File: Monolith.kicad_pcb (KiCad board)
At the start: 2 copper layers, 89.9 x 42.7 mm, 80 parts, among them IC1 HT7550-1, J1 USB_B_Micro, J2 Conn_01x11, J3 Conn_01x11, J4 Conn_01x02, J5 Conn_01x02, J6 Conn_01x07, Q1 BC818, Q2 BC818, U1 ADS1299IPAGR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

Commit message: fix pick and place stuff
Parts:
- C19, C22: footprint Capacitor_SMD:C_0603_1608Metric -> Capacitor_SMD:C_0805_2012Metric
- moved C19 1.73 mm to (232.9, 129.0)
- moved C22 1.14 mm to (202.8, 135.1)
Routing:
- net /AVSS: track 109.7 -> 98.5 mm
- net GND: track 268.6 -> 262.0 mm
- net Net-(U1-VREFN): track 9.04 -> 12.0 mm, vias 0 -> 2
- net +3V3: track 206.8 -> 208.1 mm
- net Net-(U1-VREFP): track 9.23 -> 9.80 mm
- net Net-(U1-VCAP4): track 7.40 -> 7.92 mm, vias 0 -> 2

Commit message: fix capacitor array footprint
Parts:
- C22: footprint Capacitor_SMD:C_0805_2012Metric -> Capacitor_SMD:C_0603_1608Metric
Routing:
- net /AVSS: track 98.5 -> 108.6 mm
- net /IN8P: track 19.5 -> 21.3 mm
- net GND: track 262.0 -> 263.6 mm
- net /INSRB2: track 21.9 -> 20.8 mm
- net /IN8N: track 16.9 -> 17.5 mm
- net /IN5N: track 14.6 -> 15.1 mm

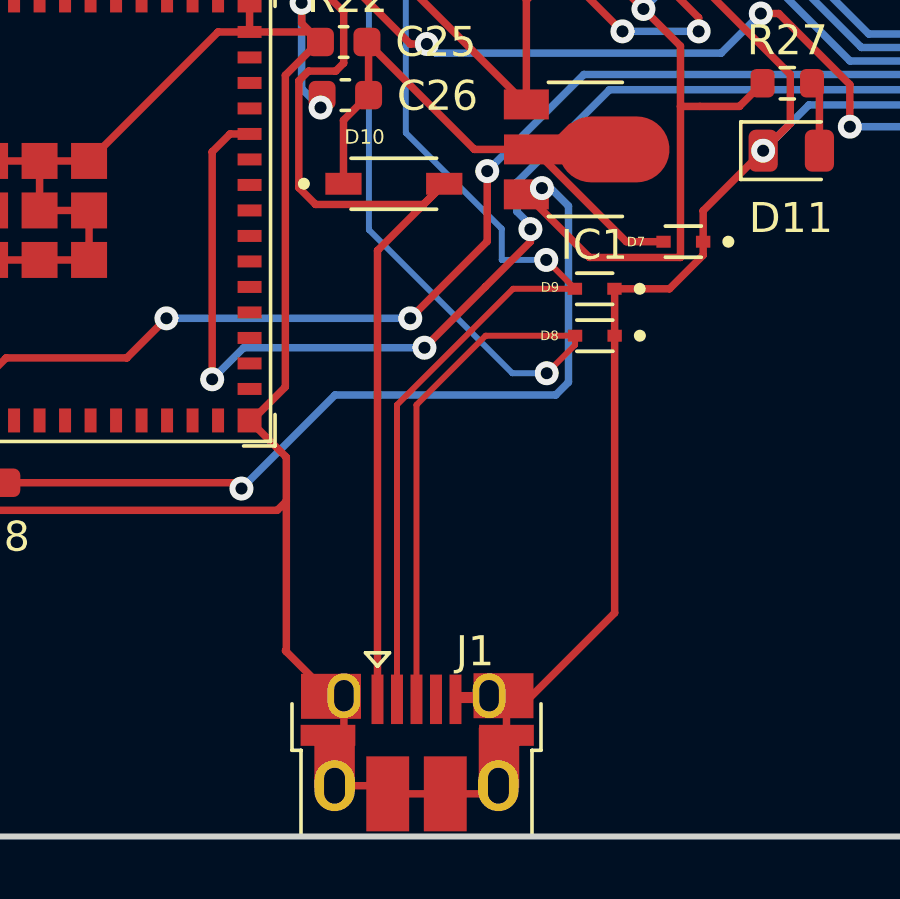
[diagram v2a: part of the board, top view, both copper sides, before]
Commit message: fix usb
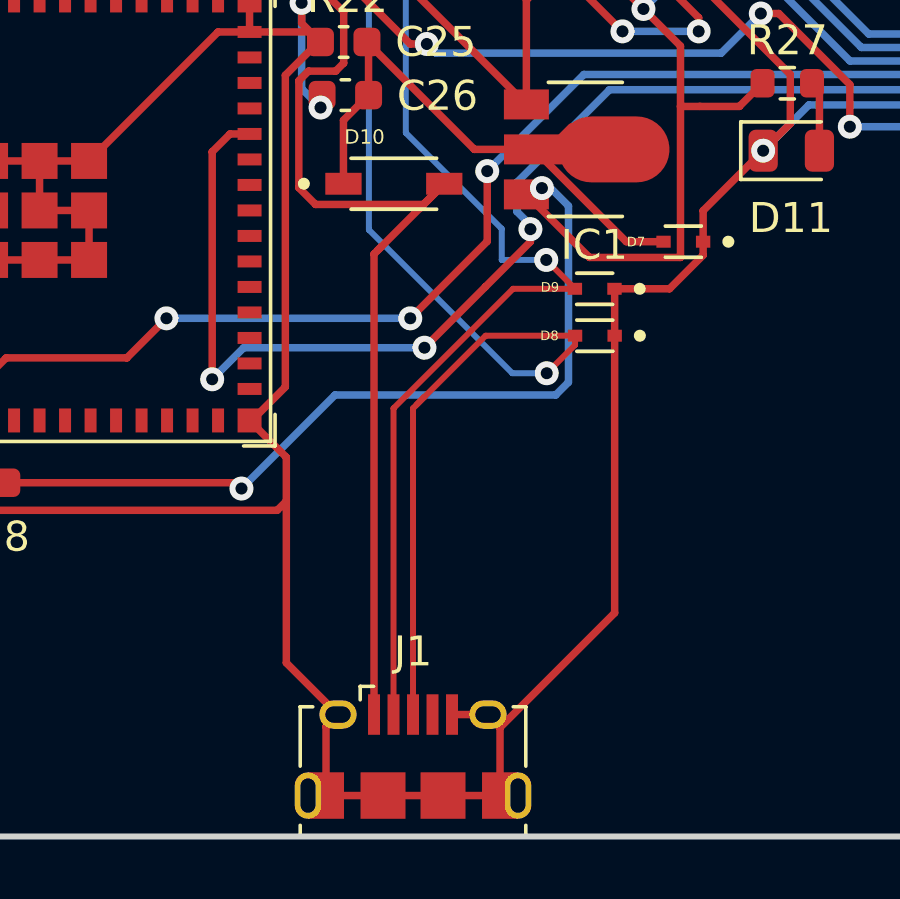
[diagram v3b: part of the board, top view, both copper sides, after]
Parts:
- J1: footprint Connector_USB:USB_Micro-B_Amphenol_10103594-0001LF_Horizontal -> Connector_USB:USB_Micro-B_Amphenol_10118194_Horizontal
- moved J1 0.20 mm to (198.9, 161.4)
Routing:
- net /USB Port/USBtoUART/DP: track 39.8 -> 40.7 mm
- net VBUS: track 35.0 -> 35.7 mm
- net GND: track 263.6 -> 262.9 mm
- net /USB Port/USBtoUART/DN: track 36.5 -> 37.0 mm

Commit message: stuff
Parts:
- removed C17: 10uF, Capacitor_SMD:C_0603_1608Metric
- removed C18: 0.1uF, Capacitor_SMD:C_0603_1608Metric
- removed J6: Conn_01x07, Connector_PinSocket_2.54mm:PinSocket_1x07_P2.54mm_Vertical
- removed U2: ESP32-S2-MINI-1, PCM_Espressif:ESP32-S2-MINI-1
- added C1: 10uF, Capacitor_SMD:C_0603_1608Metric, F.Cu at (184.3, 154.7)
- added C2: 0.1uF, Capacitor_SMD:C_0603_1608Metric, F.Cu at (182.4, 154.7)
- added J7: Conn_01x08, Connector_PinHeader_2.54mm:PinHeader_1x08_P2.54mm_Vertical, F.Cu at (218.9, 142.7)
- added U12: ESP32-S3-MINI-1, PCM_Espressif:ESP32-S3-MINI-1, F.Cu at (186.4, 144.7)
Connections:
- U1 pad 40: unconnected-(U1-SCLK-Pad40) -> /SCLK
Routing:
- net /SCLK: track 0.00 -> 60.9 mm, vias 0 -> 2
- net /DOUT: track 83.5 -> 46.1 mm, vias 5 -> 3
- net /DRDY: track 69.9 -> 87.4 mm, vias 6 -> 8
- net GND: track 262.9 -> 249.7 mm, vias 14 -> 16
- net /DIN: track 54.9 -> 42.2 mm, vias 4 -> 1
- net /GPIO1: track 67.6 -> 56.9 mm, vias 5 -> 4
- net /CS: track 66.4 -> 60.4 mm
- net /GPIO0: track 31.1 -> 32.7 mm
- net /U0RXD: track 15.0 -> 16.5 mm
- net /U0TXD: track 14.1 -> 15.6 mm
- net /EN: track 15.0 -> 16.4 mm
- net +3V3: track 208.1 -> 206.9 mm
- net /USB Port/USBtoUART/DP: track 40.7 -> 39.9 mm

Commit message: moar stuff
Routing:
- net /GPIO1: track 56.9 -> 70.1 mm, vias 4 -> 6

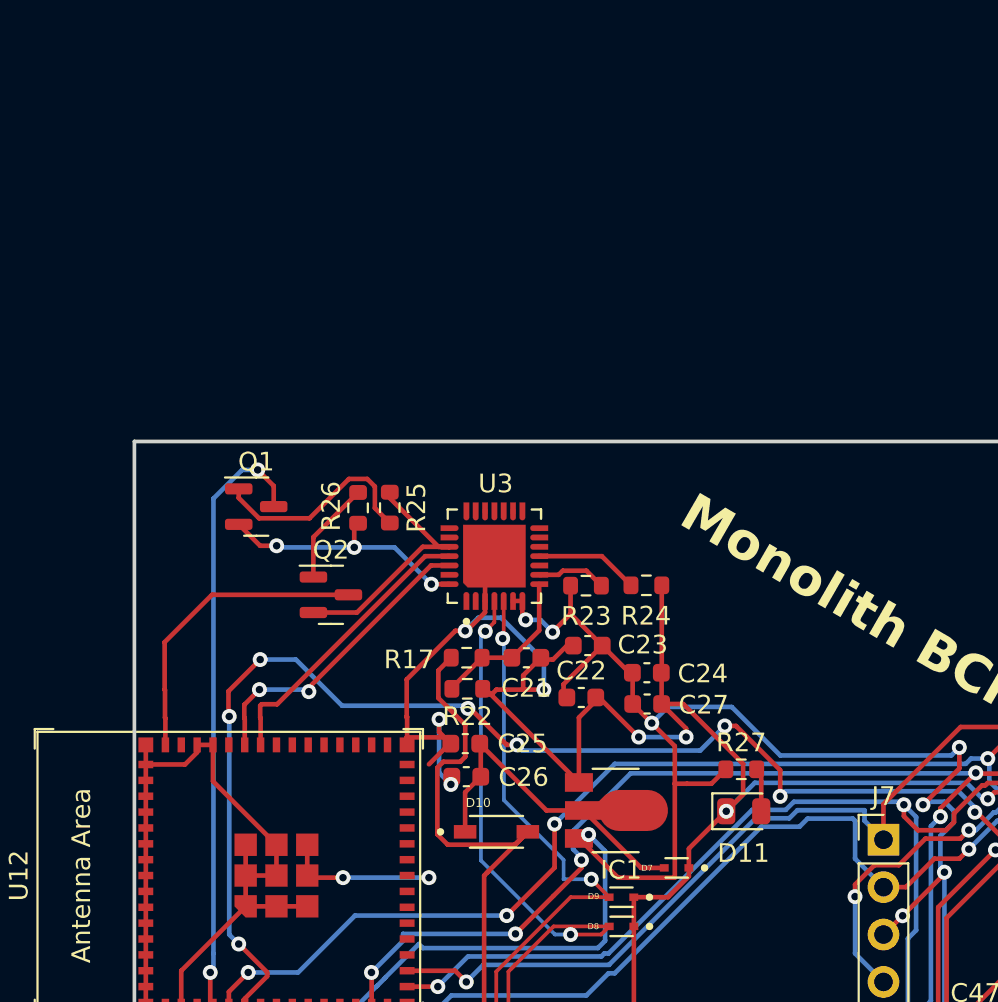
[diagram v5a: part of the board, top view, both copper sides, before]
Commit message: Replace volt reg
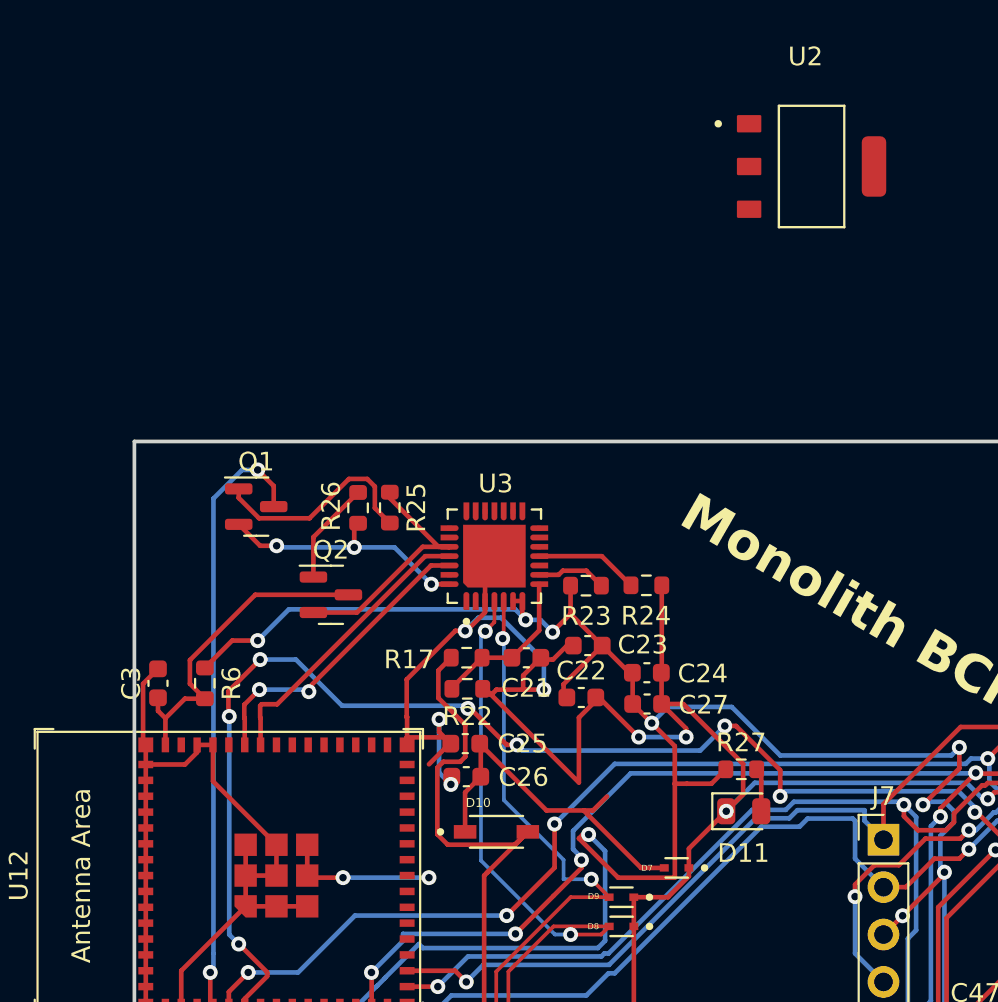
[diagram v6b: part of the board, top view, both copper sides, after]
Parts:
- removed IC1: HT7550-1, HT7550-1:SOT89
- added C3: 1uF, Capacitor_SMD:C_0603_1608Metric, F.Cu at (180.1, 134.4)
- added R6: 10k, Resistor_SMD:R_0603_1608Metric, F.Cu at (182.6, 134.4)
- added U2: AMS1117-3.3, AMS1117-3.3:SOT229P700X180-4N, F.Cu at (215.1, 106.7)
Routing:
- net +3V3: track 207.1 -> 225.8 mm, vias 14 -> 15
- net GND: track 249.7 -> 254.2 mm
- net /EN: track 16.4 -> 17.6 mm

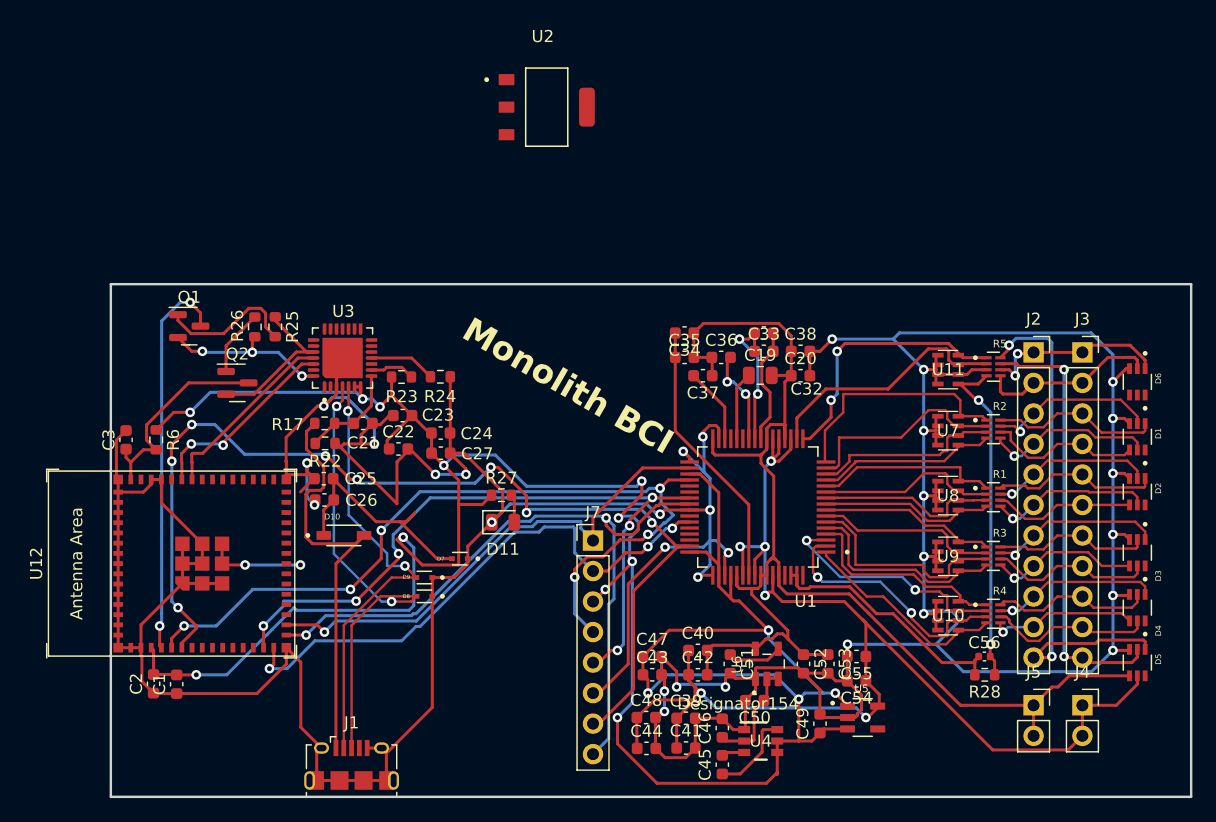
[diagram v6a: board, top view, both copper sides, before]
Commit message: fix vrm
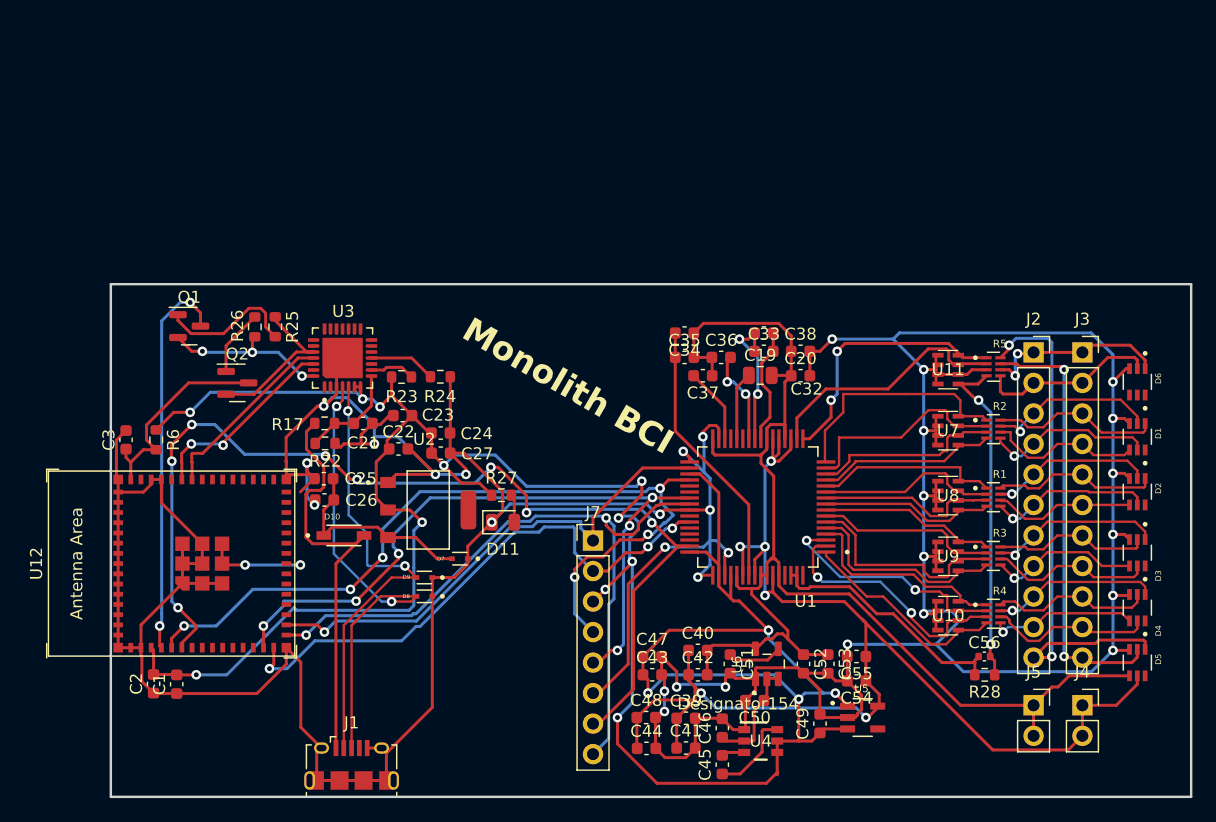
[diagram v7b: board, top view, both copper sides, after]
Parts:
- moved U2 34.9 mm to (205.2, 140.2)
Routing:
- net +3V3: track 225.8 -> 222.7 mm
- net Net-(U2-VI): track 19.3 -> 17.1 mm
- net GND: track 254.2 -> 253.1 mm
- net /USB Port/USBtoUART/DN: track 37.0 -> 38.0 mm

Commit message: add ground planes
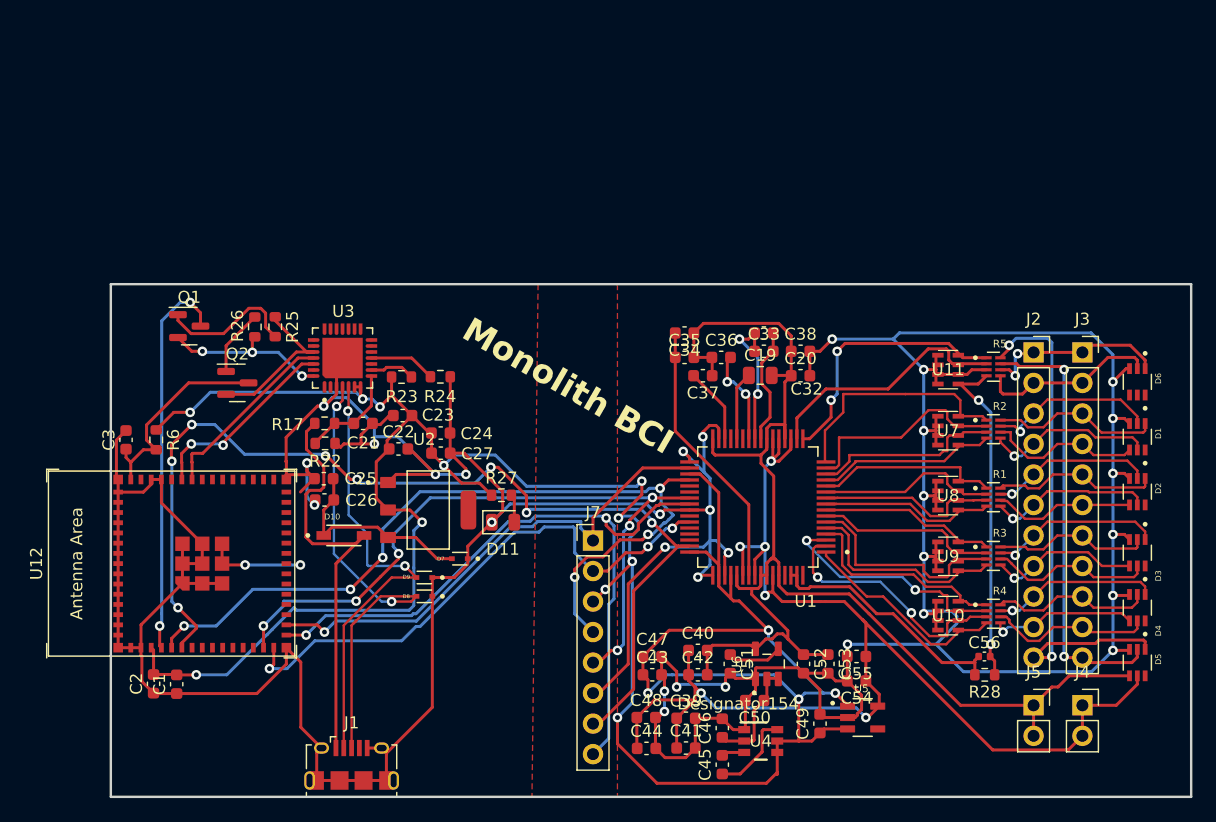
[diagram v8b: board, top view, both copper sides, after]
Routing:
- added copper zone on F.Cu, net GND
- added copper zone on F.Cu, net GNDA
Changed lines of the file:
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@@
     (fp_arc (start -0.724999 1.475002) (mid -0.778507 1.452548) (end -0.800692 1.398928)
       (stroke (width 0.127) (type solid)) (layer "F.Fab"))
-    (fp_arc (start -0.576537 -0.906071) (mid -0.449562 -1.033047) (end -0.322588 -0.906071)
+    (fp_arc (start -0.576537 -0.906071) (mid -0.449563 -1.033046) (end -0.322588 -0.906071)
       (stroke (width 0.127) (type solid)) (layer "F.Fab"))
     (fp_arc (start -0.322588 -0.906071) (mid -0.449563 -0.7791) (end -0.576537 -0.906071)
@@
   (segment (start 204.216 148.844) (end 211.9105 141.1495) (width 0.25) (layer "B.Cu") (net 111))
   (segment (start 213.713256 141.1495) (end 214.146756 140.716) (width 0.25) (layer "B.Cu") (net 111))
+  (zone (net 1) (net_name "GNDA") (layer "F.Cu") (hatch edge 0.5)
+    (connect_pads (clearance 0.5))
+    (min_thickness 0.25) (filled_areas_thickness no)
+    (fill yes (thermal_gap 0.5) (thermal_bridge_width 0.5))
+    (polygon
+      (pts
+        (xy 220.98 121.412)
+        (xy 220.98 164.084)
+        (xy 268.732 164.084)
+        (xy 268.732 121.412)
+      )
+    )
+  )
+  (zone (net 35) (net_name "GND") (layer "F.Cu") (hatch edge 0.5)
+    (priority 1)
+    (connect_pads (clearance 0.5))
+    (min_thickness 0.25) (filled_areas_thickness no)
+    (fill yes (thermal_gap 0.5) (thermal_bridge_width 0.5))
+    (polygon
+      (pts
+        (xy 178.816 121.412)
+        (xy 214.376 121.412)
+        (xy 213.868 164.084)
+        (xy 178.816 164.084)
+      )
+    )
+  )
 )
